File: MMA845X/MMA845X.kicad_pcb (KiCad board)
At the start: 2 copper layers, 25.4 x 17.8 mm, 24 parts, among them J1 Conn_01x06, J2 Conn_01x04, J3 Conn_01x06, J4 Conn_01x04, Q2 BSS138DW, U1 AP2127K-3.3, U2 MMA8451

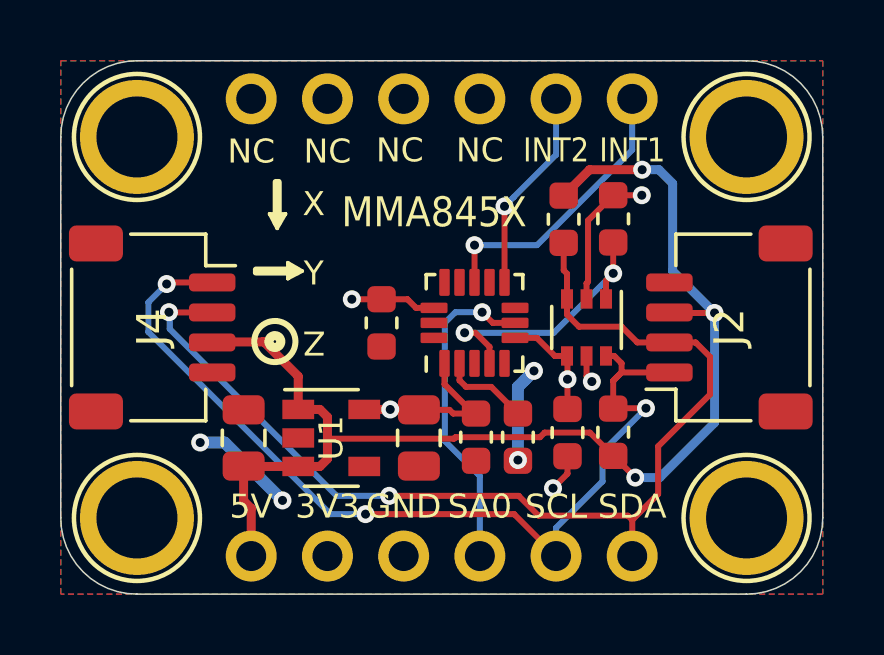
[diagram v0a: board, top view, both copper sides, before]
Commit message: MMA845X PCB and SCH edit
Extra Power Pins Added
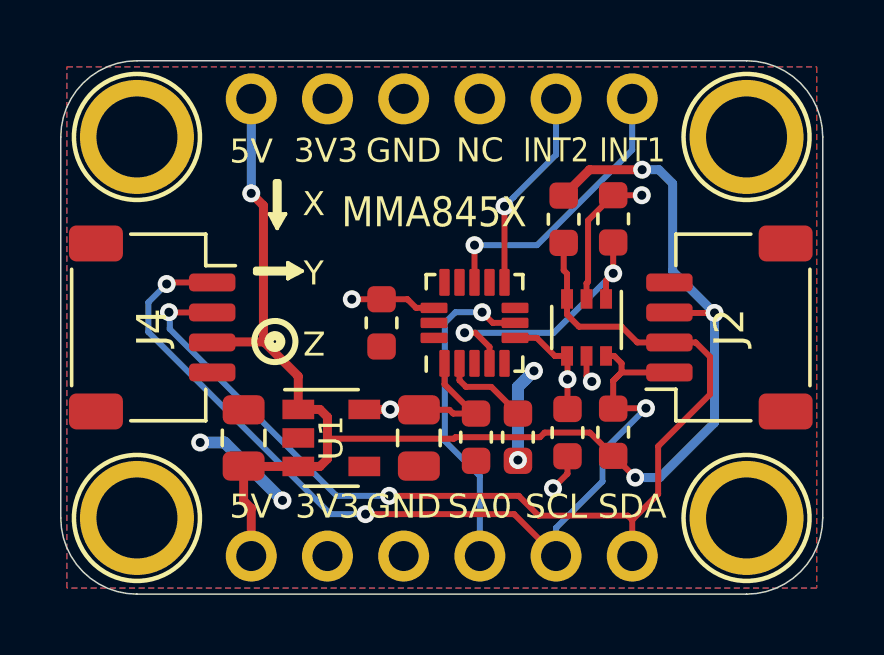
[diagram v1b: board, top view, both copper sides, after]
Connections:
- J3 pad 1: Net-(J3-Pad1) -> 5V
- J3 pad 2: Net-(J3-Pad2) -> 3V3
- J3 pad 3: Net-(J3-Pad3) -> GND
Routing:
- net 5V: track 41.5 -> 49.8 mm, vias 3 -> 4
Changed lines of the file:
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@@
     (thickness 1.6)
     (drawings 56)
-    (tracks 167)
+    (tracks 172)
     (zones 0)
     (modules 24)
-    (nets 22)
+    (nets 19)
   )
   (page User 132.004 102.006)
@@
     (34 B.Paste user hide)
     (35 F.Paste user hide)
-    (36 B.SilkS user)
+    (36 B.SilkS user hide)
     (37 F.SilkS user)
     (38 B.Mask user hide)
@@
   )
   (setup
-    (last_trace_width 0.4)
+    (last_trace_width 0.3)
     (user_trace_width 0.2)
     (user_trace_width 0.25)
@@
   (net 12 INT1)
   (net 13 INT2)
-  (net 14 "Net-(J3-Pad3)")
-  (net 15 "Net-(J3-Pad2)")
-  (net 16 "Net-(J3-Pad1)")
-  (net 17 "Net-(U2-Pad16)")
-  (net 18 "Net-(U2-Pad15)")
-  (net 19 "Net-(U2-Pad13)")
-  (net 20 "Net-(U2-Pad8)")
-  (net 21 "Net-(U2-Pad3)")
+  (net 14 "Net-(U2-Pad16)")
+  (net 15 "Net-(U2-Pad15)")
+  (net 16 "Net-(U2-Pad13)")
+  (net 17 "Net-(U2-Pad8)")
+  (net 18 "Net-(U2-Pad3)")
   (net_class Default "This is the default net class."
     (clearance 0.127)
@@
     (add_net INT2)
     (add_net "Net-(C3-Pad1)")
-    (add_net "Net-(J3-Pad1)")
-    (add_net "Net-(J3-Pad2)")
-    (add_net "Net-(J3-Pad3)")
     (add_net "Net-(J3-Pad4)")
     (add_net "Net-(U1-Pad4)")
@@
     (fp_line (start 2.1 -2.1) (end -2.1 -2.1) (layer F.CrtYd) (width 0.05))
     (pad 16 smd roundrect (at -0.5 -1.35 90) (size 0.35 0.9) (layers F.Cu F.Paste F.Mask) (roundrect_rratio 0.15)
-      (net 17 "Net-(U2-Pad16)"))
+      (net 14 "Net-(U2-Pad16)"))
     (pad 15 smd roundrect (at 0 -1.35 90) (size 0.35 0.9) (layers F.Cu F.Paste F.Mask) (roundrect_rratio 0.15)
-      (net 18 "Net-(U2-Pad15)"))
+      (net 15 "Net-(U2-Pad15)"))
     (pad 14 smd roundrect (at 0.5 -1.35 90) (size 0.35 0.9) (layers F.Cu F.Paste F.Mask) (roundrect_rratio 0.15)
       (net 3 3V3))
     (pad 13 smd roundrect (at 1.35 -1) (size 0.35 0.9) (layers F.Cu F.Paste F.Mask) (roundrect_rratio 0.15)
-      (net 19 "Net-(U2-Pad13)"))
+      (net 16 "Net-(U2-Pad13)"))
     (pad 12 smd roundrect (at 1.35 -0.5) (size 0.35 0.9) (layers F.Cu F.Paste F.Mask) (roundrect_rratio 0.15)
       (net 1 GND))
@@
       (net 13 INT2))
     (pad 8 smd roundrect (at 0.5 1.35 270) (size 0.35 0.9) (layers F.Cu F.Paste F.Mask) (roundrect_rratio 0.15)
-      (net 20 "Net-(U2-Pad8)"))
+      (net 17 "Net-(U2-Pad8)"))
     (pad 7 smd roundrect (at 0 1.35 270) (size 0.35 0.9) (layers F.Cu F.Paste F.Mask) (roundrect_rratio 0.15)
       (net 11 SA0))
@@
       (net 8 SCL_3V3))
     (pad 3 smd roundrect (at -1.35 0 180) (size 0.35 0.9) (layers F.Cu F.Paste F.Mask) (roundrect_rratio 0.15)
-      (net 21 "Net-(U2-Pad3)"))
+      (net 18 "Net-(U2-Pad3)"))
     (pad 2 smd roundrect (at -1.35 -0.5 180) (size 0.35 0.9) (layers F.Cu F.Paste F.Mask) (roundrect_rratio 0.15)
       (net 10 "Net-(C3-Pad1)"))
@@
       (net 9 "Net-(J3-Pad4)"))
     (pad 3 thru_hole oval (at 0 -5.08 270) (size 1.7 1.7) (drill 1) (layers *.Cu *.Mask)
-      (net 14 "Net-(J3-Pad3)"))
+      (net 1 GND))
     (pad 2 thru_hole oval (at 0 -2.54 270) (size 1.7 1.7) (drill 1) (layers *.Cu *.Mask)
-      (net 15 "Net-(J3-Pad2)"))
+      (net 3 3V3))
     (pad 1 thru_hole circle (at 0 0 270) (size 1.7 1.7) (drill 1) (layers *.Cu *.Mask)
-      (net 16 "Net-(J3-Pad1)"))
+      (net 2 5V))
     (model ${KISYS3DMOD}/Connector_PinHeader_2.54mm.3dshapes/PinHeader_1x06_P2.54mm_Vertical.wrl
       (at (xyz 0 0 0))
@@
     (effects (font (size 1 0.9) (thickness 0.13)))
   )
-  (gr_text NC (at 58.928 30.099) (layer F.SilkS)
+  (gr_text 5V (at 58.928 30.099) (layer F.SilkS)
     (effects (font (size 0.8 0.8) (thickness 0.12)))
   )
-  (gr_text NC (at 61.468 30.099) (layer F.SilkS)
+  (gr_text 3V3 (at 61.4172 30.0736) (layer F.SilkS)
     (effects (font (size 0.8 0.8) (thickness 0.12)))
   )
-  (gr_text NC (at 63.881 30.0609) (layer F.SilkS)
+  (gr_text GND (at 64.008 30.0736) (layer F.SilkS)
     (effects (font (size 0.8 0.8) (thickness 0.12)))
   )
@@
   (segment (start 70.2182 39.4716) (end 70.993 40.2464) (width 0.2) (layer F.Cu) (net 2))
   (segment (start 68.707 39.4716) (end 70.2182 39.4716) (width 0.2) (layer F.Cu) (net 2))
+  (segment (start 59.3344 36.449) (end 59.3344 31.9024) (width 0.3) (layer F.Cu) (net 2))
+  (segment (start 59.3344 31.9024) (end 58.928 31.496) (width 0.3) (layer F.Cu) (net 2))
+  (segment (start 58.928 31.496) (end 58.928 31.496) (width 0.3) (layer F.Cu) (net 2))
+  (via (at 58.928 31.496) (size 0.6) (drill 0.3) (layers F.Cu B.Cu) (net 2))
+  (segment (start 58.928 31.496) (end 58.928 28.3464) (width 0.3) (layer B.Cu) (net 2))
   (segment (start 64.5035 38.6994) (end 64.516 38.7119) (width 0.3) (layer F.Cu) (net 3))
   (segment (start 62.695 38.6994) (end 63.561 38.6994) (width 0.3) (layer F.Cu) (net 3))
@@
     (polygon
       (pts
-        (xy 52.578 27.0764) (xy 77.978 27.0764) (xy 77.978 44.8564) (xy 52.578 44.8564)
+        (xy 52.7812 27.2796) (xy 77.7748 27.2796) (xy 77.7748 44.6532) (xy 52.7812 44.6532)
       )
     )
@@
     (polygon
       (pts
-        (xy 52.578 27.0764) (xy 77.978 27.0764) (xy 77.978 44.8564) (xy 52.578 44.8564)
+        (xy 52.7812 27.2796) (xy 77.7748 27.2796) (xy 77.7748 44.6532) (xy 52.7812 44.6532)
       )
     )

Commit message: MMA845X Update
MMA8453 Added - 10 Bit Version
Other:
- board text added: "10 Bit 12 Bit 14 Bit"
- board text removed: "12 Bit 14 Bit"
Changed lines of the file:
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@@
   (general
     (thickness 1.6)
-    (drawings 56)
+    (drawings 57)
     (tracks 172)
     (zones 0)
@@
     (date 2020-01-22)
     (rev 2)
-    (company SirBoard)
-    (comment 1 "1.56Hz - 800Hz Data Rates")
-    (comment 2 "±2g, ±4g, ±8g")
-    (comment 3 "Digital 8bit/12Bit or 14bit I2C Accelerometer")
-    (comment 4 "MMA8451, MMA8452 - SirBlue")
+    (company "SirBoard ")
+    (comment 1 "Digital 10 Bit, 8bit/12Bit or 14bit I2C Accelerometer")
+    (comment 2 "1.56Hz - 800Hz Data Rates")
+    (comment 3 "Accelerometer: ±2g, ±4g, ±8g")
+    (comment 4 "MMA8451, MMA8452, MMA8453 - SirBlue")
   )
   (layers
@@
     (34 B.Paste user hide)
     (35 F.Paste user hide)
-    (36 B.SilkS user hide)
+    (36 B.SilkS user)
     (37 F.SilkS user)
     (38 B.Mask user hide)
@@
   )
   (setup
-    (last_trace_width 0.3)
+    (last_trace_width 0.127)
     (user_trace_width 0.2)
     (user_trace_width 0.25)
@@
     )
   )
-  (gr_text "12 Bit\n14 Bit" (at 70.1294 34.7472) (layer B.SilkS)
+  (gr_line (start 67.8815 32.3215) (end 74.0791 32.3215) (layer B.SilkS) (width 0.12))
+  (gr_text "10 Bit\n12 Bit\n14 Bit" (at 70.1929 34.6075) (layer B.SilkS)
     (effects (font (size 0.9 0.9) (thickness 0.13)) (justify mirror))
   )
-  (gr_line (start 67.818 33.1978) (end 74.0156 33.1978) (layer B.SilkS) (width 0.12))
-  (gr_line (start 74.0156 33.1978) (end 74.0156 36.1442) (layer B.SilkS) (width 0.12))
-  (gr_line (start 74.0156 36.1442) (end 67.818 36.1442) (layer B.SilkS) (width 0.12))
-  (gr_line (start 67.818 36.1442) (end 67.818 33.1978) (layer B.SilkS) (width 0.12))
-  (gr_line (start 67.818 34.7472) (end 74.0156 34.7472) (layer B.SilkS) (width 0.12))
-  (gr_line (start 72.517 33.1978) (end 72.517 36.1442) (layer B.SilkS) (width 0.12))
+  (gr_line (start 67.8815 33.8455) (end 74.0791 33.8455) (layer B.SilkS) (width 0.12))
+  (gr_line (start 74.0791 32.3215) (end 74.0791 36.7665) (layer B.SilkS) (width 0.12))
+  (gr_line (start 74.0791 36.7665) (end 67.8815 36.7665) (layer B.SilkS) (width 0.12))
+  (gr_line (start 67.8815 36.7665) (end 67.8815 32.3215) (layer B.SilkS) (width 0.12))
+  (gr_line (start 67.8815 35.306) (end 74.0791 35.306) (layer B.SilkS) (width 0.12))
+  (gr_line (start 72.5805 32.3215) (end 72.5805 36.7665) (layer B.SilkS) (width 0.12))
   (gr_text MMA845X (at 65.024 32.131) (layer F.SilkS)
     (effects (font (size 1 0.9) (thickness 0.13)))
@@
   )
   (dimension 15.24 (width 0.15) (layer Dwgs.User)
-    (gr_text "15.240 mm" (at 84.1294 35.9664 270) (layer Dwgs.User)
-      (effects (font (size 1 1) (thickness 0.15)))
-    )
-    (feature1 (pts (xy 71.628 43.5864) (xy 83.415821 43.5864)))
-    (feature2 (pts (xy 71.628 28.3464) (xy 83.415821 28.3464)))
-    (crossbar (pts (xy 82.8294 28.3464) (xy 82.8294 43.5864)))
-    (arrow1a (pts (xy 82.8294 43.5864) (xy 82.242979 42.459896)))
-    (arrow1b (pts (xy 82.8294 43.5864) (xy 83.415821 42.459896)))
-    (arrow2a (pts (xy 82.8294 28.3464) (xy 82.242979 29.472904)))
-    (arrow2b (pts (xy 82.8294 28.3464) (xy 83.415821 29.472904)))
+    (gr_text "15.240 mm" (at 84.1294 35.8775 270) (layer Dwgs.User)
+      (effects (font (size 1 1) (thickness 0.15)))
+    )
+    (feature1 (pts (xy 71.628 43.4975) (xy 83.415821 43.4975)))
+    (feature2 (pts (xy 71.628 28.2575) (xy 83.415821 28.2575)))
+    (crossbar (pts (xy 82.8294 28.2575) (xy 82.8294 43.4975)))
+    (arrow1a (pts (xy 82.8294 43.4975) (xy 82.242979 42.370996)))
+    (arrow1b (pts (xy 82.8294 43.4975) (xy 83.415821 42.370996)))
+    (arrow2a (pts (xy 82.8294 28.2575) (xy 82.242979 29.384004)))
+    (arrow2b (pts (xy 82.8294 28.2575) (xy 83.415821 29.384004)))
   )
   (dimension 17.78 (width 0.15) (layer Dwgs.User)

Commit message: Soldermask width adjusted
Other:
- rule solder_mask_min_width: 0.1 -> 0.05
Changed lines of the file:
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@@
     (pad_drill 1)
     (pad_to_mask_clearance 0)
-    (solder_mask_min_width 0.1)
+    (solder_mask_min_width 0.05)
     (aux_axis_origin 0 0)
     (visible_elements 7FFFFFFF)
